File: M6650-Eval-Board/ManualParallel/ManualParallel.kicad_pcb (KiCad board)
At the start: 2 copper layers, 39.4 x 22.2 mm, 12 parts, among them J1 Parallel, SW1 SW_DIP_x04, SW2 SW_DIP_x04, SW3 SW_Push, SW4 SW_Push

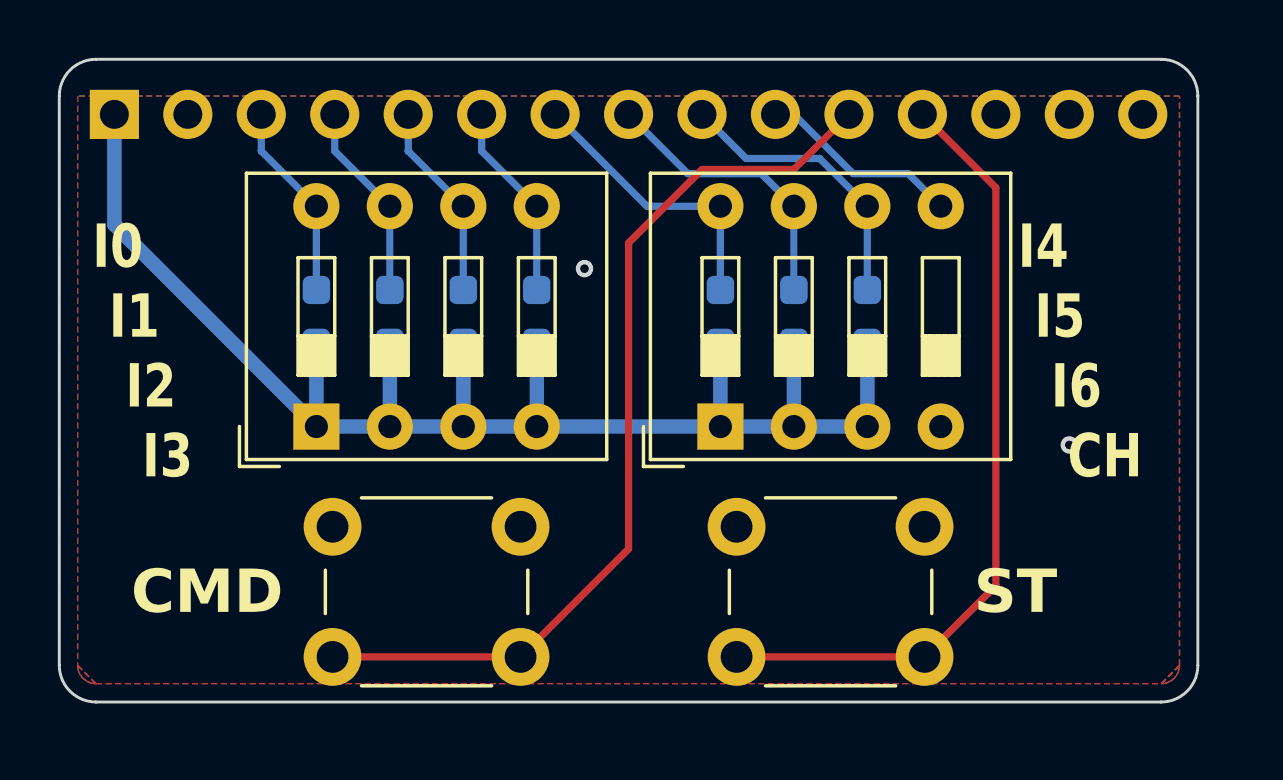
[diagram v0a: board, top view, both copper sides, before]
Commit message: Fix a dumb error on eval board extras
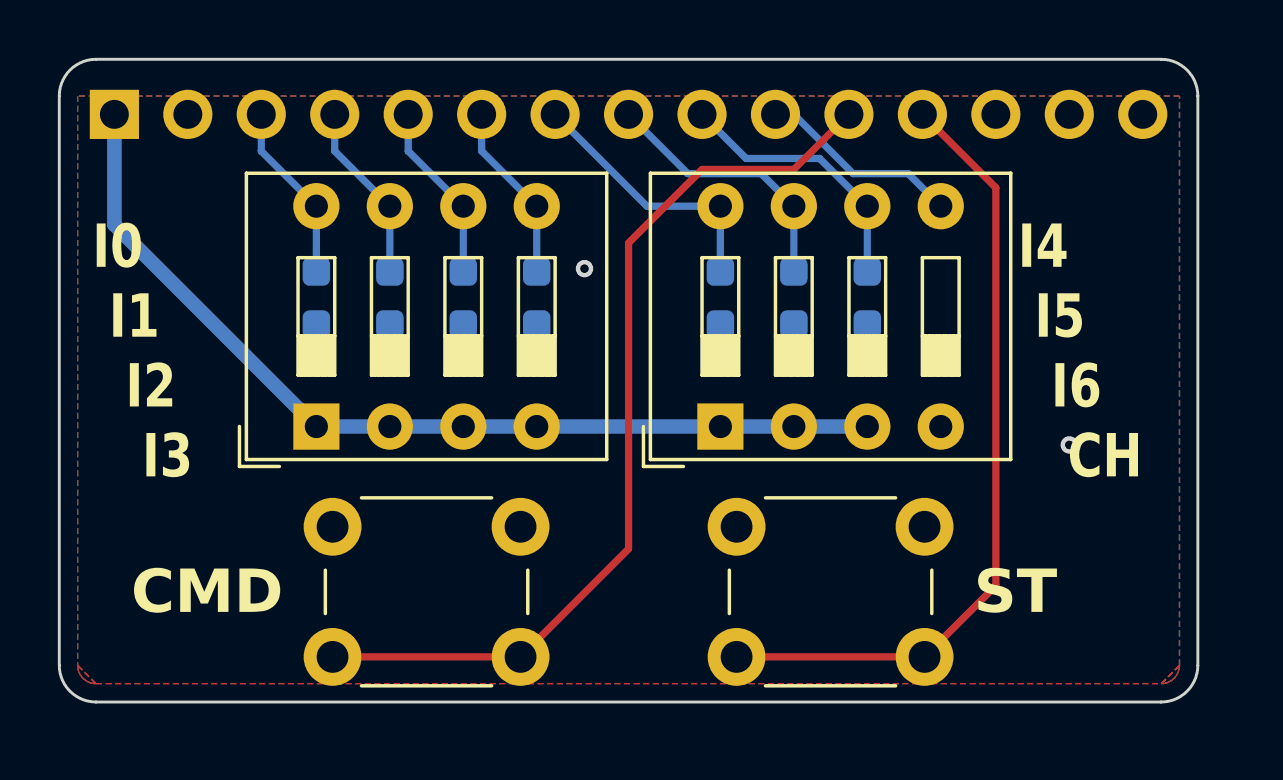
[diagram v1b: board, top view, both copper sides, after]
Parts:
- moved R1 0.64 mm to (22.2, 21.6)
- moved R2 0.64 mm to (24.8, 21.6)
- moved R3 0.64 mm to (27.3, 21.6)
- moved R4 0.64 mm to (29.8, 21.6)
- moved R5 0.64 mm to (36.2, 21.6)
- moved R6 0.64 mm to (38.7, 21.6)
- moved R7 0.64 mm to (41.3, 21.6)
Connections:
- R1 pad 1: /5V -> /GND
- R2 pad 1: /5V -> /GND
- R3 pad 1: /5V -> /GND
- R4 pad 1: /5V -> /GND
- R5 pad 1: /5V -> /GND
- R6 pad 1: /5V -> /GND
- R7 pad 1: /5V -> /GND
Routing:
- net /5V: track 53.0 -> 32.7 mm
- net /I6: track 9.93 -> 9.29 mm
- net /I5: track 9.93 -> 9.29 mm
- net /I4: track 9.93 -> 9.29 mm
- net /I3: track 6.86 -> 6.23 mm
- net /I2: track 6.86 -> 6.23 mm
- net /I1: track 6.86 -> 6.23 mm
- net /I0: track 6.86 -> 6.23 mm

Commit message: Add debounce to manual parallel board, redo board edges and clearance rules
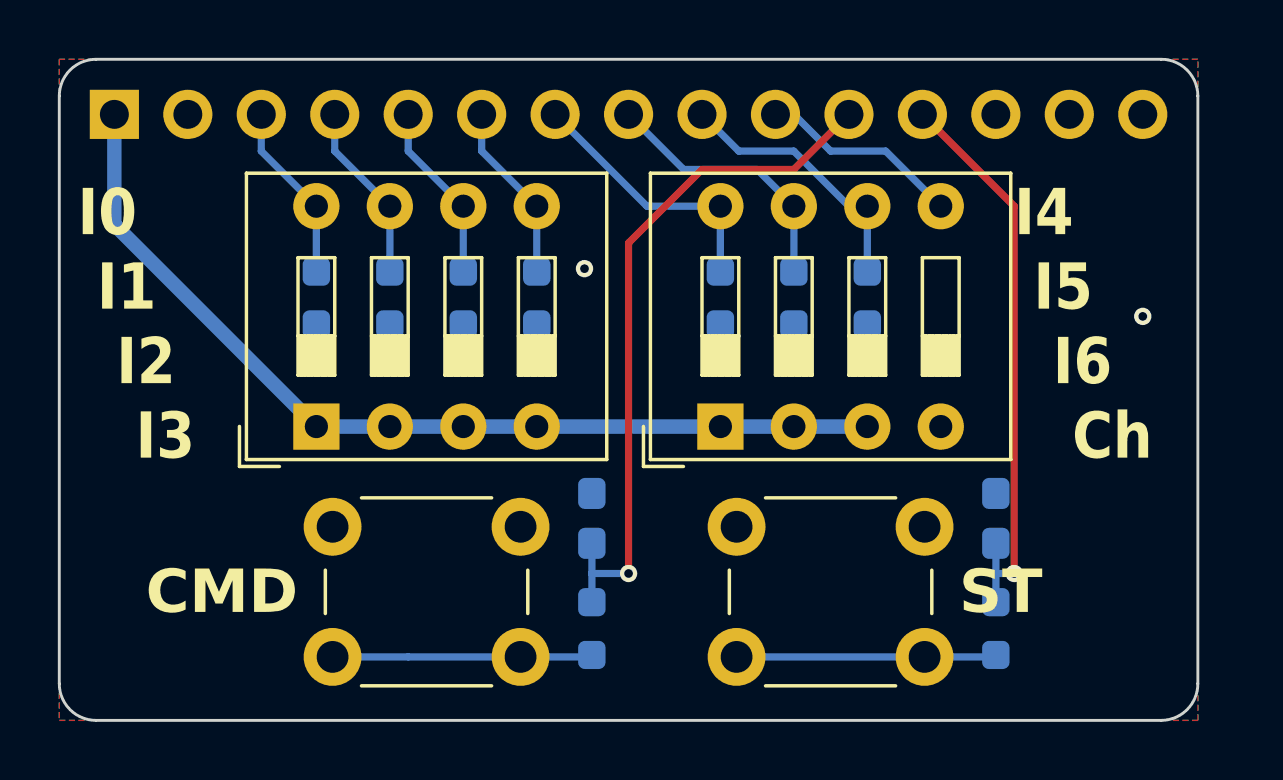
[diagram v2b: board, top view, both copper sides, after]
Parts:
- added C1: 100n, Capacitor_SMD:C_0603_1608Metric_Pad1.08x0.95mm_HandSolder, B.Cu at (31.8, 29.2)
- added C2: 100n, Capacitor_SMD:C_0603_1608Metric_Pad1.08x0.95mm_HandSolder, B.Cu at (45.7, 29.2)
- added R8: 1K, Resistor_SMD:R_0603_1608Metric_Pad0.98x0.95mm_HandSolder, B.Cu at (31.8, 33.0)
- added R9: 1K, Resistor_SMD:R_0603_1608Metric_Pad0.98x0.95mm_HandSolder, B.Cu at (45.7, 33.0)
- J1: footprint Connector_PinSocket_2.54mm:PinSocket_1x15_P2.54mm_Vertical -> Connector_PinHeader_2.54mm:PinHeader_1x15_P2.54mm_Vertical
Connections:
- SW3 pad 2: /CMD -> Net-(R8-Pad1)
- SW4 pad 2: /ST -> Net-(R9-Pad1)
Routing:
- net Net-(R8-Pad1): track 0.00 -> 8.99 mm
- net Net-(R9-Pad1): track 0.00 -> 8.99 mm
- net /CMD: track 31.8 -> 24.2 mm, vias 0 -> 1
- net /ST: track 27.3 -> 19.9 mm, vias 0 -> 1
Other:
- board size 39.4 x 22.2 mm -> 39.4 x 22.9 mm
- board text added: "I4 I5 I6 Ch"
- board text removed: "I4 I5 I6 CH"
